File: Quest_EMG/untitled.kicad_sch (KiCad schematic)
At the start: 52 parts, among them IC1 OPA2890IDGST, U1 AD8620, U2 INA121UAE4

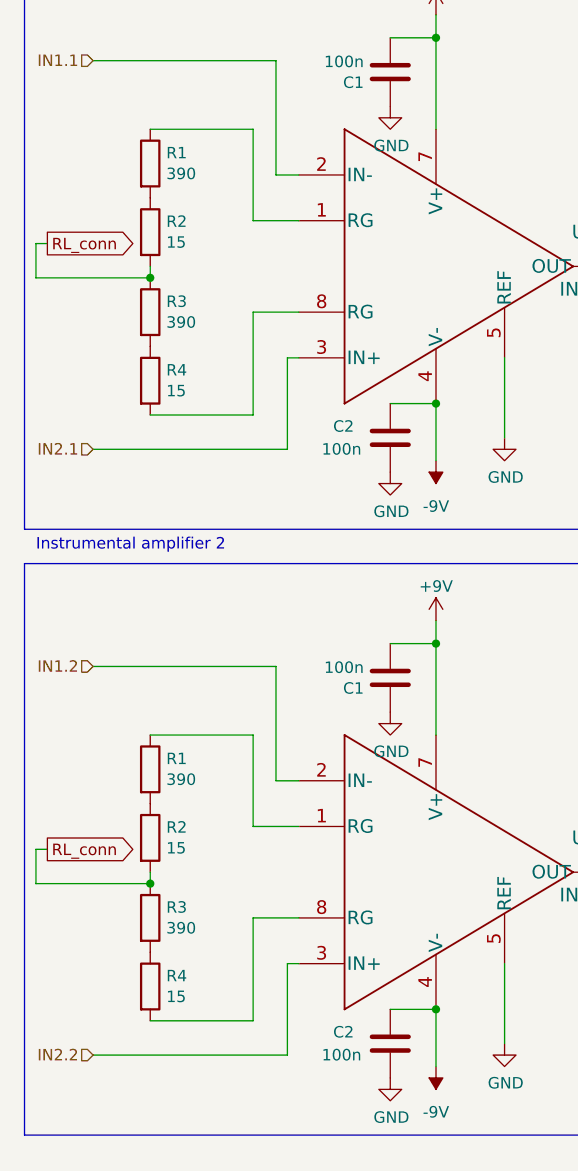
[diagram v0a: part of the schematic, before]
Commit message: 62 times amplification
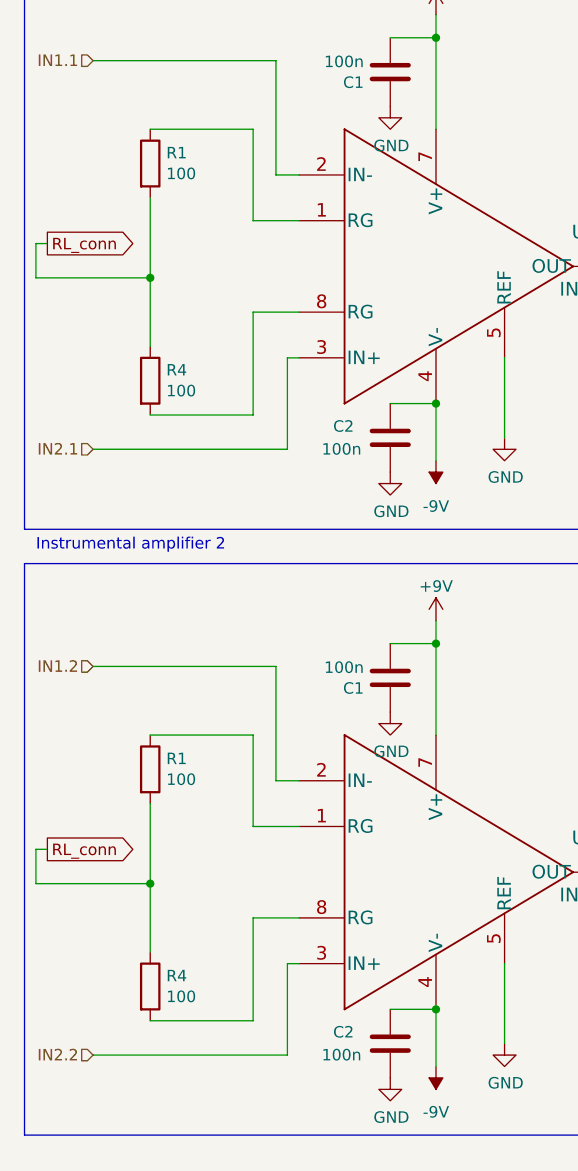
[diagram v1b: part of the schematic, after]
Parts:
- removed R2 (x2): 15, Resistor_SMD:R_0402_1005Metric, symbol Device:R
- removed R3 (x2): 390, Resistor_SMD:R_0402_1005Metric, symbol Device:R
- R1: value 390 -> 100
- R4: value 15 -> 100
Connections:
- net RL_conn: now also R1.2, R1.2, R4.1, R4.1
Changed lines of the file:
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@@
 (kicad_sch (version 20230121) (generator eeschema)
   (paper "A4")
-  (junction (at 46.99 54.61) (diameter 0) (color 0 0 0 0)
-  )
   (junction (at 78.74 135.89) (diameter 0) (color 0 0 0 0)
   )
@@
   (junction (at 204.47 45.72) (diameter 0) (color 0 0 0 0)
   )
+  (junction (at 46.99 54.61) (diameter 0) (color 0 0 0 0)
+  )
   (junction (at 208.28 38.1) (diameter 0) (color 0 0 0 0)
   )
@@
   (junction (at 78.74 27.94) (diameter 0) (color 0 0 0 0)
   )
+  (junction (at 46.99 121.92) (diameter 0) (color 0 0 0 0)
+  )
   (junction (at 80.01 181.61) (diameter 0) (color 0 0 0 0)
   )
@@
   (junction (at 204.47 62.23) (diameter 0) (color 0 0 0 0)
   )
-  (junction (at 46.99 121.92) (diameter 0) (color 0 0 0 0)
-  )
   (junction (at 78.74 68.58) (diameter 0) (color 0 0 0 0)
   )
@@
     (stroke (width 0) (type default))
   )
+  (wire (pts (xy 46.99 54.61) (xy 46.99 62.23))
+    (stroke (width 0) (type default))
+  )
   (wire (pts (xy 204.47 38.1) (xy 204.47 43.18))
     (stroke (width 0) (type default))
@@
     (stroke (width 0) (type default))
   )
-  (wire (pts (xy 46.99 121.92) (xy 46.99 120.65))
+  (wire (pts (xy 46.99 113.03) (xy 46.99 121.92))
+    (stroke (width 0) (type default))
+  )
+  (wire (pts (xy 46.99 121.92) (xy 46.99 129.54))
     (stroke (width 0) (type default))
   )
@@
     (stroke (width 0) (type default))
   )
-  (wire (pts (xy 46.99 54.61) (xy 46.99 53.34))
+  (wire (pts (xy 46.99 45.72) (xy 46.99 54.61))
     (stroke (width 0) (type default))
   )
@@
       (effects (font (size 1.27 1.27)) (justify left))
     )
-    (property "Value" "390" (at 48.768 43.053 0)
+    (property "Value" "100" (at 48.768 43.053 0)
       (effects (font (size 1.27 1.27)) (justify left))
     )
@@
     )
   )
-  (symbol (lib_id "Device:R") (at 46.99 125.73 0) (unit 1)
-    (in_bom yes) (on_board yes) (dnp no)
-    (property "Reference" "R3" (at 48.768 124.5616 0)
-      (effects (font (size 1.27 1.27)) (justify left))
-    )
-    (property "Value" "390" (at 48.768 126.873 0)
-      (effects (font (size 1.27 1.27)) (justify left))
-    )
-    (property "Footprint" "Resistor_SMD:R_0402_1005Metric" (at 45.212 125.73 90)
-      (effects (font (size 1.27 1.27)) hide)
-    )
-    (property "Datasheet" "~" (at 46.99 125.73 0)
-      (effects (font (size 1.27 1.27)) hide)
-    )
-    (pin "1")
-    (pin "2")
-    (instances
-      (project "Quest_EMG_V2"
-        (path "/0a1c0da6-b5f4-4811-bab6-325eaaab9ba6"
-          (reference "R3") (unit 1)
-        )
-        (path "/0a1c0da6-b5f4-4811-bab6-325eaaab9ba6/838164a3-69ca-4a23-b38f-f69071e638d3"
-          (reference "R18") (unit 1)
-        )
-      )
-      (project "Quest_EMG"
-        (path "/67748ae8-7ff0-411f-94ce-ac7b136b3c1f"
-          (reference "R3") (unit 1)
-        )
-        (path "/67748ae8-7ff0-411f-94ce-ac7b136b3c1f/8e7c5476-16bd-404a-9f48-60ae4ce6d75c"
-          (reference "R7") (unit 1)
-        )
-      )
-      (project "HARDIMPL"
-        (path "/acefa769-b849-43b8-9ddb-a217494d9f73"
-          (reference "R3") (unit 1)
-        )
-      )
-    )
-  )
   (symbol (lib_id "power:GND") (at 220.98 64.77 0) (unit 1)
     (in_bom yes) (on_board yes) (dnp no)
@@
       (effects (font (size 1.27 1.27)) (justify left))
     )
-    (property "Value" "15" (at 48.768 134.493 0)
+    (property "Value" "100" (at 48.768 134.493 0)
       (effects (font (size 1.27 1.27)) (justify left))
     )
@@
     )
   )
-  (symbol (lib_id "Device:R") (at 46.99 58.42 0) (unit 1)
-    (in_bom yes) (on_board yes) (dnp no)
-    (property "Reference" "R3" (at 48.768 57.2516 0)
-      (effects (font (size 1.27 1.27)) (justify left))
-    )
-    (property "Value" "390" (at 48.768 59.563 0)
-      (effects (font (size 1.27 1.27)) (justify left))
-    )
-    (property "Footprint" "Resistor_SMD:R_0402_1005Metric" (at 45.212 58.42 90)
-      (effects (font (size 1.27 1.27)) hide)
-    )
-    (property "Datasheet" "~" (at 46.99 58.42 0)
-      (effects (font (size 1.27 1.27)) hide)
-    )
-    (pin "1")
-    (pin "2")
-    (instances
-      (project "Quest_EMG_V2"
-        (path "/0a1c0da6-b5f4-4811-bab6-325eaaab9ba6"
-          (reference "R3") (unit 1)
-        )
-        (path "/0a1c0da6-b5f4-4811-bab6-325eaaab9ba6/838164a3-69ca-4a23-b38f-f69071e638d3"
-          (reference "R3") (unit 1)
-        )
-      )
-      (project "Quest_EMG"
-        (path "/67748ae8-7ff0-411f-94ce-ac7b136b3c1f"
-          (reference "R3") (unit 1)
-        )
-        (path "/67748ae8-7ff0-411f-94ce-ac7b136b3c1f/8e7c5476-16bd-404a-9f48-60ae4ce6d75c"
-          (reference "R3") (unit 1)
-        )
-      )
-      (project "HARDIMPL"
-        (path "/acefa769-b849-43b8-9ddb-a217494d9f73"
-          (reference "R3") (unit 1)
-        )
-      )
-    )
-  )
   (symbol (lib_id "Device:R") (at 220.98 60.96 0) (unit 1)
     (in_bom yes) (on_board yes) (dnp no)
@@
     )
   )
-  (symbol (lib_id "Device:R") (at 46.99 49.53 0) (unit 1)
-    (in_bom yes) (on_board yes) (dnp no)
-    (property "Reference" "R2" (at 48.768 48.3616 0)
-      (effects (font (size 1.27 1.27)) (justify left))
-    )
-    (property "Value" "15" (at 48.768 50.673 0)
-      (effects (font (size 1.27 1.27)) (justify left))
-    )
-    (property "Footprint" "Resistor_SMD:R_0402_1005Metric" (at 45.212 49.53 90)
-      (effects (font (size 1.27 1.27)) hide)
-    )
-    (property "Datasheet" "~" (at 46.99 49.53 0)
-      (effects (font (size 1.27 1.27)) hide)
-    )
-    (pin "1")
-    (pin "2")
-    (instances
-      (project "Quest_EMG_V2"
-        (path "/0a1c0da6-b5f4-4811-bab6-325eaaab9ba6"
-          (reference "R2") (unit 1)
-        )
-        (path "/0a1c0da6-b5f4-4811-bab6-325eaaab9ba6/838164a3-69ca-4a23-b38f-f69071e638d3"
-          (reference "R2") (unit 1)
-        )
-      )
-      (project "Quest_EMG"
-        (path "/67748ae8-7ff0-411f-94ce-ac7b136b3c1f"
-          (reference "R2") (unit 1)
-        )
-        (path "/67748ae8-7ff0-411f-94ce-ac7b136b3c1f/8e7c5476-16bd-404a-9f48-60ae4ce6d75c"
-          (reference "R2") (unit 1)
-        )
-      )
-      (project "HARDIMPL"
-        (path "/acefa769-b849-43b8-9ddb-a217494d9f73"
-          (reference "R2") (unit 1)
-        )
-      )
-    )
-  )
   (symbol (lib_id "power:GND") (at 233.68 101.6 0) (unit 1)
     (in_bom yes) (on_board yes) (dnp no)
@@
       (effects (font (size 1.27 1.27)) (justify left))
     )
-    (property "Value" "390" (at 48.768 110.363 0)
+    (property "Value" "100" (at 48.768 110.363 0)
       (effects (font (size 1.27 1.27)) (justify left))
     )
@@
       (effects (font (size 1.27 1.27)) (justify left))
     )
-    (property "Value" "15" (at 48.768 67.183 0)
+    (property "Value" "100" (at 48.768 67.183 0)
       (effects (font (size 1.27 1.27)) (justify left))
     )
@@
         )
       )
-    )
-  )
-  (symbol (lib_id "Device:R") (at 46.99 116.84 0) (unit 1)
-    (in_bom yes) (on_board yes) (dnp no)
-    (property "Reference" "R2" (at 48.768 115.6716 0)
-      (effects (font (size 1.27 1.27)) (justify left))
-    )
-    (property "Value" "15" (at 48.768 117.983 0)
-      (effects (font (size 1.27 1.27)) (justify left))
-    )
-    (property "Footprint" "Resistor_SMD:R_0402_1005Metric" (at 45.212 116.84 90)
-      (effects (font (size 1.27 1.27)) hide)
-    )
-    (property "Datasheet" "~" (at 46.99 116.84 0)
-      (effects (font (size 1.27 1.27)) hide)
-    )
-    (pin "1")
-    (pin "2")
-    (instances
-      (project "Quest_EMG_V2"
-        (path "/0a1c0da6-b5f4-4811-bab6-325eaaab9ba6"
-          (reference "R2") (unit 1)
-        )
-        (path "/0a1c0da6-b5f4-4811-bab6-325eaaab9ba6/838164a3-69ca-4a23-b38f-f69071e638d3"
-          (reference "R17") (unit 1)
-        )
-      )
-      (project "Quest_EMG"
-        (path "/67748ae8-7ff0-411f-94ce-ac7b136b3c1f"
-          (reference "R2") (unit 1)
-        )
-        (path "/67748ae8-7ff0-411f-94ce-ac7b136b3c1f/8e7c5476-16bd-404a-9f48-60ae4ce6d75c"
-          (reference "R6") (unit 1)
-        )
-      )
-      (project "HARDIMPL"
-        (path "/acefa769-b849-43b8-9ddb-a217494d9f73"
-          (reference "R2") (unit 1)
-        )
-      )

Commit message: forgot something
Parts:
- removed C3 (x2), C4 (x2), C5 (x2): 390n, Capacitor_SMD:C_0402_1005Metric, symbol Device:C
- removed R10 (x2), R11 (x2), R12 (x2), R13 (x2), R15 (x2): 10k, Resistor_SMD:R_0402_1005Metric, symbol Device:R
- removed R14 (x2): 5k8, Resistor_SMD:R_0402_1005Metric, symbol Device:R
- removed R8 (x2): 33k, Resistor_SMD:R_0402_1005Metric, symbol Device:R
- removed R9 (x2): 56k, Resistor_SMD:R_0402_1005Metric, symbol Device:R
- added R8 (x4): 1K, Resistor_SMD:R_0402_1005Metric, symbol Device:R
- added R8 (x2), R9 (x2): 15K, Resistor_SMD:R_0402_1005Metric, symbol Device:R
- added R8 (x3): 68k, Resistor_SMD:R_0402_1005Metric, symbol Device:R
- added R8: 56k, Resistor_SMD:R_0402_1005Metric, symbol Device:R
- added R8 (x2): 10K, Resistor_SMD:R_0402_1005Metric, symbol Device:R
- added R9: 15k, Resistor_SMD:R_0402_1005Metric, symbol Device:R
- added R9: 33k, Resistor_SMD:R_0402_1005Metric, symbol Device:R
- R8: value 33k -> 68k
- R8: value 33k -> 56k
- R9: value 56k -> 33k
- R9: value 56k -> 15k
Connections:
- net +9V: now also R8.1, R8.1, R8.1
- net -9V: now also R8.1
- net 32: now also IC1.7 (OUT_B), R8.2; no longer IC1.6 (-IN_B)
- net 33: now also IC1.7 (OUT_B), R8.1; no longer IC1.6 (-IN_B)
- net GND: now also R9.2, R9.2, R9.2, R9.2
- net In_amp1: now also R8.2
- net In_amp2: now also R8.2
- net at IC1.9 (OUT_A): now also R8.1 (x2)
- net at IC1.10 (-IN_A): now also R8.1, R8.2, R8.2 (x2)
- net at IC1.3 (-VS): now also R8.2, R9.1
- net at IC1.5 (+IN_B): now also R8.2, R9.1 (x2)
- net at IC1.8 (+VS): now also R8.2, R9.1
- new net: IC1.6 (-IN_B), R8.1, R8.1
- new net: IC1.6 (-IN_B), R8.1, R8.2
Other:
- note added: "capacitors and resistors for Fc van 10kHz"
- note removed: "new capacitors and resistors for Fc van 10kHz"
- moved on the sheet: R8, R9
